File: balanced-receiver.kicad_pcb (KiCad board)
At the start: 2 copper layers, 52.5 x 40 mm, 54 parts, among them J1 NC3FAH2, J2 Barrel_Jack_Switch, J3 Screw_Terminal_01x02, J4 Screw_Terminal_01x02, J5 Screw_Terminal_01x02, J6 Screw_Terminal_01x02, J7 Screw_Terminal_01x02, J8 Conn_01x02_Pin, Q1 Q_PMOS_GDS, U1 THAT1240, U2 TPS62932, U3 LM2776

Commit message: Added DRC pipeline action
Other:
- board text added: "${COMMENT8} ${COMMENT9} ${REVISION} ${CURRENT_DATE}"
- board text removed: "Balanced Receiver ${COMMENT1} ${REVISION} ${CURRENT_DATE}"
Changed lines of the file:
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@@
 	(paper "A5")
 	(title_block
-		(title "Balanced Receiver")
-		(date "2025.01.31")
-		(rev "v1.0")
-		(company "Filip Tefr")
-		(comment 1 "github.com/brbcza")
+		(title "${TITLE_BLOCK_PROJECT_NAME}")
+		(date "${TITLE_BLOCK_DATE}")
+		(rev "${TITLE_BLOCK_REVISION}")
+		(company "${TITLE_BLOCK_AUTHOR}")
+		(comment 1 "${TITLE_BLOCK_REPOSITORY}")
+		(comment 8 "${TITLE_BLOCK_PROJECT_NAME_SHORT}")
+		(comment 9 "${TITLE_BLOCK_BASE_REPOSITORY}")
 	)
 	(layers
@@
 		(tags "neutrik xlr a")
 		(property "Reference" "J1"
-			(at 1.7 -8.1 360)
+			(at 1.7 -8.1 0)
 			(layer "F.SilkS")
 			(effects
@@
 		)
 		(property "Value" "NC3FAH2"
-			(at 4.3 18 360)
+			(at 4.3 18 0)
 			(layer "F.Fab")
 			(hide yes)
@@
 		)
 		(fp_text user "${REFERENCE}"
-			(at 10.35 3.81 360)
+			(at 10.35 3.81 0)
 			(layer "F.Fab")
 			(effects
@@
 		)
 	)
-	(gr_text "Balanced  Receiver\n${COMMENT1}\n${REVISION}  ${CURRENT_DATE}\n"
+	(gr_text "${COMMENT8}\n${COMMENT9}\n${REVISION}  ${CURRENT_DATE}\n"
 		(at 80.5325 53.44 0)
 		(layer "F.SilkS" knockout)

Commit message: Added release action
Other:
- board text added: "${COMMENT8} ${COMMENT9} ${REVISION} ${ISSUE_DATE}"
- board text removed: "${COMMENT8} ${COMMENT9} ${REVISION} ${CURRENT_DATE}"
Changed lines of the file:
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@@
 		)
 	)
-	(gr_text "${COMMENT8}\n${COMMENT9}\n${REVISION}  ${CURRENT_DATE}\n"
+	(gr_text "${COMMENT8}\n${COMMENT9}\n${REVISION} ${ISSUE_DATE}\n"
 		(at 80.5325 53.44 0)
 		(layer "F.SilkS" knockout)

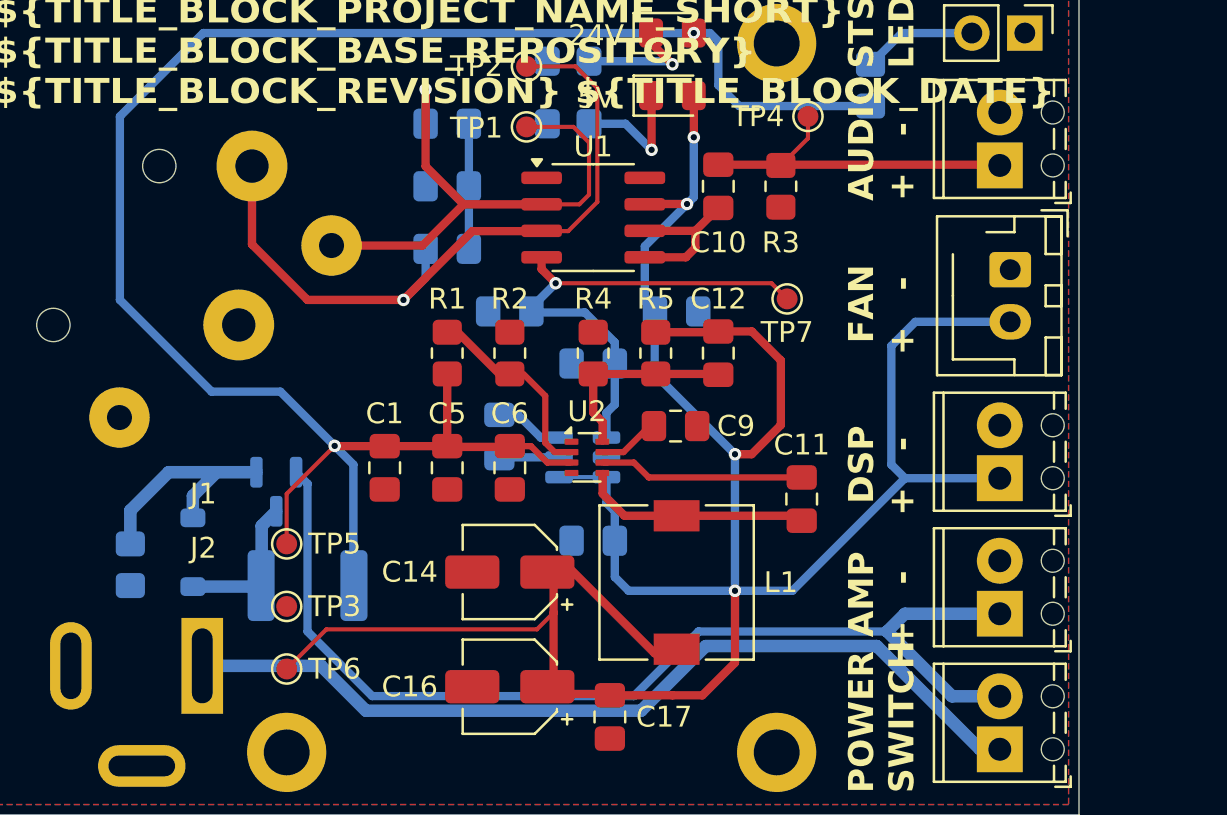
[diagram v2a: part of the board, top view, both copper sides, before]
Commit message: Added local component library
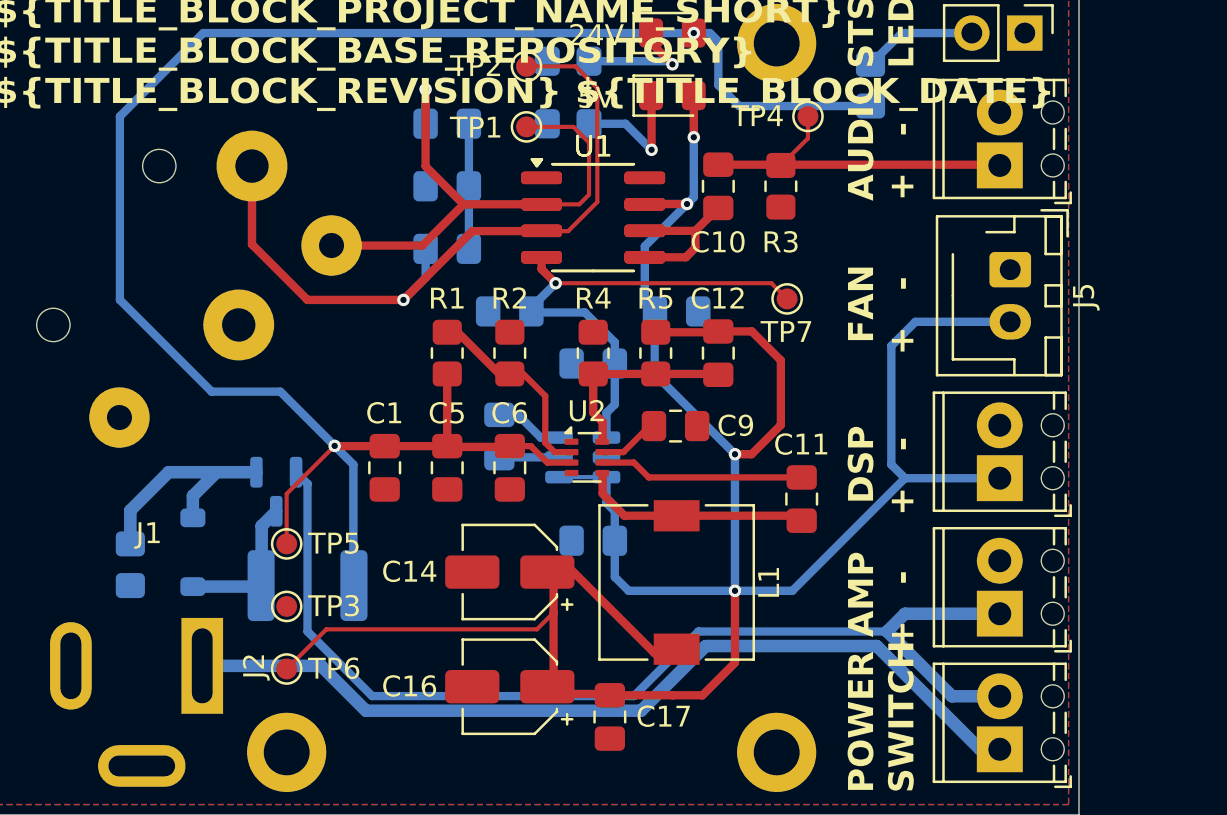
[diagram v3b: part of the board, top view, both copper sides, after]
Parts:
- added U1: THAT1240, Package_SO:SOIC-8_3.9x4.9mm_P1.27mm, F.Cu at (109.3, 58.8)
- F1: footprint brbCZa-KicadFootprintLib:Fuse_1812_4532Metric_Pad1.30x3.40mm_HandSolder -> balanced-receiver:Fuse_1812_4532Metric_Pad1.30x3.40mm_HandSolder
- J1: footprint brbCZa-KicadFootprintLib:Jack_XLR_Neutrik_NC3FAH2_Horizontal -> balanced-receiver:Jack_XLR_Neutrik_NC3FAH2_Horizontal
- J2: footprint brbCZa-KicadFootprintLib:BarrelJack_GCT_DCJ200-10-A_Horizontal -> balanced-receiver:BarrelJack_GCT_DCJ200-10-A_Horizontal
- J5: footprint brbCZa-KicadFootprintLib:JST_XH_B2B-XH-AM_1x02_P2.50mm_Vertical -> balanced-receiver:JST_XH_B2B-XH-AM_1x02_P2.50mm_Vertical
- L1: footprint brbCZa-KicadFootprintLib:L_7.3x7.3_H4.5 -> balanced-receiver:L_7.3x7.3_H4.5
- U2: footprint brbCZa-KicadFootprintLib:SOT-583-8 -> balanced-receiver:SOT-583-8

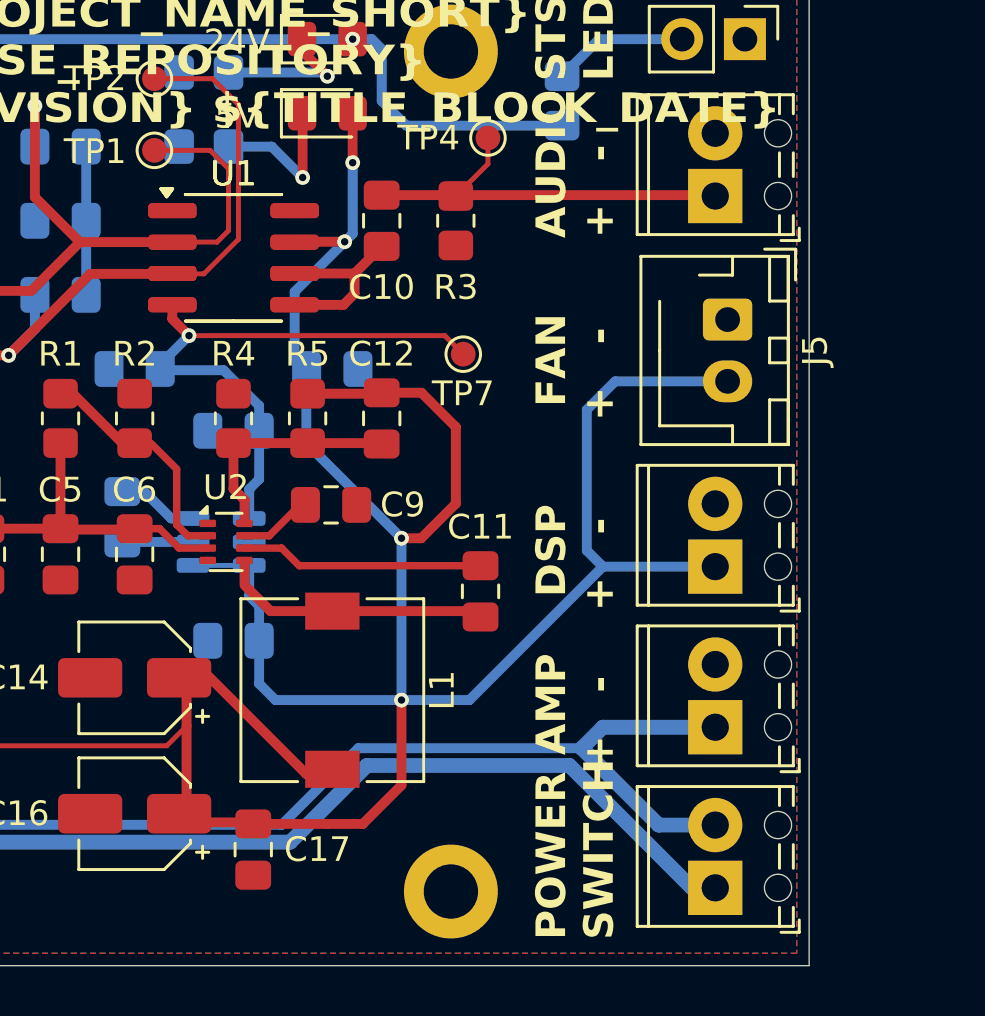
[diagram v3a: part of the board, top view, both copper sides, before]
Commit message: Fixed DRC and ERC errors
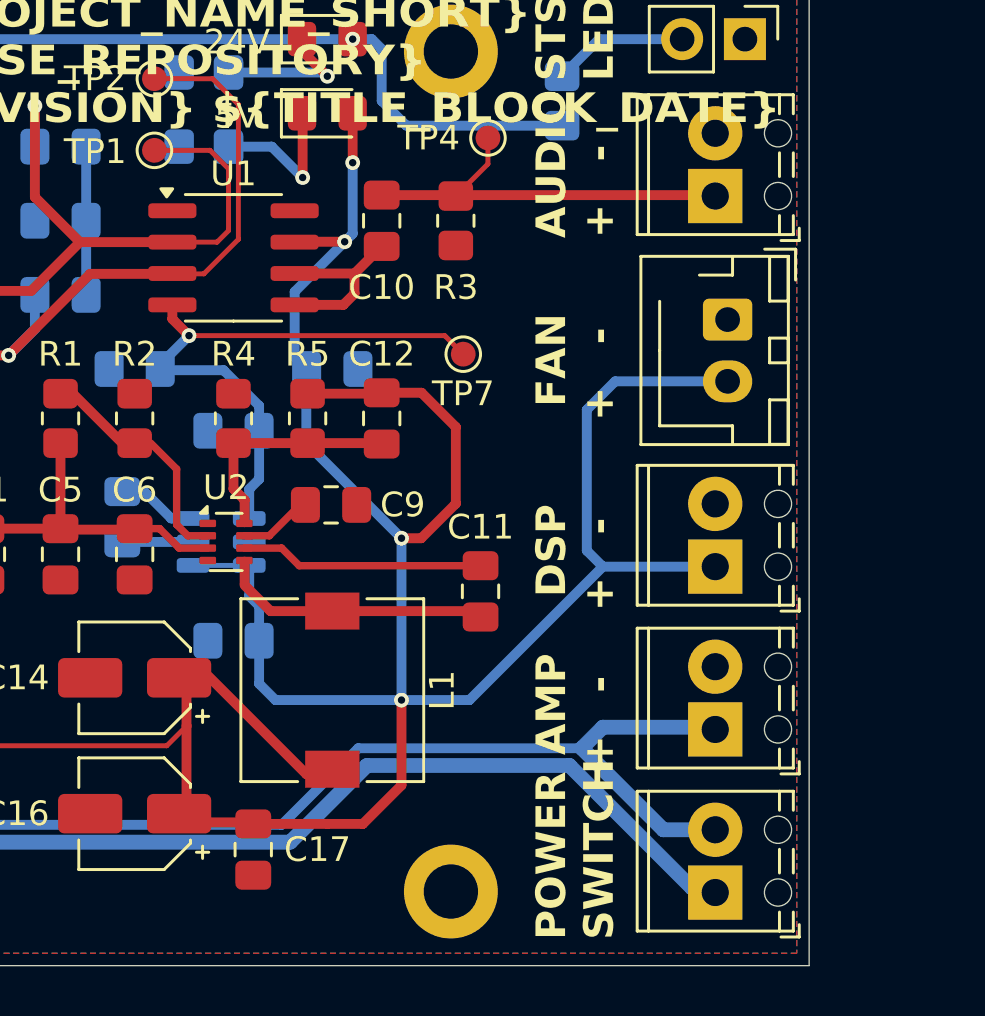
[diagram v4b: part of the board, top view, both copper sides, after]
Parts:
- removed the U1 at (109.3, 58.8)
- moved J3 0.19 mm to (128.8, 84.5)
- moved J4 0.09 mm to (128.8, 77.9)

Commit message: WIP: Converting to schematic
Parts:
- removed the C10 at (115.3, 57.3)
- removed the C4 at (102.3, 60.3)
- removed the C8 at (105.3, 63.3)
- removed D3: LED, LED_SMD:LED_0805_2012Metric_Pad1.15x1.40mm_HandSolder
- removed the J1 at (92.3, 63.9)
- removed J5: Screw_Terminal_01x02, balanced-receiver:JST_XH_B2B-XH-AM_1x02_P2.50mm_Vertical
- removed J8: Conn_01x02_Pin, Connector_PinHeader_2.54mm:PinHeader_1x02_P2.54mm_Vertical
- removed the R3 at (118.3, 57.3)
- removed the R7 at (122.6, 52.4)
- removed R9: 330Ω, Resistor_SMD:R_0805_2012Metric_Pad1.20x1.40mm_HandSolder
- removed the REF** at (118.1, 50.4)
- removed TP1: Audio+, TestPoint:TestPoint_Pad_D1.0mm
- removed the TP2 at (106.1, 51.5)
- removed TP3, TP7: -5V, TestPoint:TestPoint_Pad_D1.0mm
- removed TP4: AudioOut, TestPoint:TestPoint_Pad_D1.0mm
- removed TP6: +5V, TestPoint:TestPoint_Pad_D1.0mm
- added C17: 47pF, Capacitor_SMD:C_0805_2012Metric_Pad1.18x1.45mm_HandSolder, B.Cu at (28.4, 87.9)
- added C18: 470pF, Capacitor_SMD:C_0805_2012Metric_Pad1.18x1.45mm_HandSolder, B.Cu at (28.4, 85.4)
- added C19: 470pF, Capacitor_SMD:C_0805_2012Metric_Pad1.18x1.45mm_HandSolder, B.Cu at (28.4, 90.4)
- added C20: 100nF, Capacitor_SMD:C_0805_2012Metric_Pad1.18x1.45mm_HandSolder, F.Cu at (34.4, 80.4)
- added C21: 100nF, Capacitor_SMD:C_0805_2012Metric_Pad1.18x1.45mm_HandSolder, F.Cu at (34.4, 82.9)
- added C22: 1uF, Capacitor_SMD:C_0805_2012Metric_Pad1.18x1.45mm_HandSolder, F.Cu at (32.4, 69.9)
- added C23: 22pF, Capacitor_SMD:C_0805_2012Metric_Pad1.18x1.45mm_HandSolder, F.Cu at (57.4, 76.0)
- added C24: 22pF, Capacitor_SMD:C_0805_2012Metric_Pad1.18x1.45mm_HandSolder, F.Cu at (57.4, 71.9)
- added C25: 3.3nF, Capacitor_SMD:C_0805_2012Metric_Pad1.18x1.45mm_HandSolder, F.Cu at (60.9, 69.4)
- added C26: 56nF, Capacitor_SMD:C_0805_2012Metric_Pad1.18x1.45mm_HandSolder, F.Cu at (54.4, 66.9)
- added C27: 10uF, Capacitor_SMD:C_0805_2012Metric_Pad1.18x1.45mm_HandSolder, B.Cu at (42.9, 82.9)
- added C28: 100nF, Capacitor_SMD:C_0805_2012Metric_Pad1.18x1.45mm_HandSolder, F.Cu at (37.1, 75.4)
- added C29: 100nF, Capacitor_SMD:C_0805_2012Metric_Pad1.18x1.45mm_HandSolder, F.Cu at (39.4, 72.4)
- added C30: 100nF, Capacitor_SMD:C_0805_2012Metric_Pad1.18x1.45mm_HandSolder, B.Cu at (42.9, 75.4)
- added C31: 10uF, Capacitor_SMD:C_0805_2012Metric_Pad1.18x1.45mm_HandSolder, B.Cu at (42.9, 69.4)
- added C32: 100nF, Capacitor_SMD:C_0805_2012Metric_Pad1.18x1.45mm_HandSolder, B.Cu at (42.9, 77.9)
- added C33: 100nF, Capacitor_SMD:C_0805_2012Metric_Pad1.18x1.45mm_HandSolder, B.Cu at (42.9, 66.9)
- added C34: 100nF, Capacitor_SMD:C_0805_2012Metric_Pad1.18x1.45mm_HandSolder, B.Cu at (42.9, 80.4)
- added C35: 100nF, Capacitor_SMD:C_0805_2012Metric_Pad1.18x1.45mm_HandSolder, B.Cu at (47.4, 77.9)
- added C36: 10uF, Capacitor_SMD:C_0805_2012Metric_Pad1.18x1.45mm_HandSolder, B.Cu at (47.4, 80.4)
- added C37: 100nF, Capacitor_SMD:C_0805_2012Metric_Pad1.18x1.45mm_HandSolder, B.Cu at (54.4, 66.9)
- added C38: 100nF, Capacitor_SMD:C_0805_2012Metric_Pad1.18x1.45mm_HandSolder, B.Cu at (49.9, 66.9)
- added C39: 10uF, Capacitor_SMD:C_0805_2012Metric_Pad1.18x1.45mm_HandSolder, B.Cu at (54.4, 69.4)
- added C40: 10uF, Capacitor_SMD:C_0805_2012Metric_Pad1.18x1.45mm_HandSolder, B.Cu at (49.9, 69.4)
- added C41: 1uF, Capacitor_SMD:C_0805_2012Metric_Pad1.18x1.45mm_HandSolder, F.Cu at (28.9, 61.8)
- added C42: 1uF, Capacitor_SMD:C_0805_2012Metric_Pad1.18x1.45mm_HandSolder, F.Cu at (63.9, 57.3)
- added C43: 820pF, Capacitor_SMD:C_0805_2012Metric_Pad1.18x1.45mm_HandSolder, F.Cu at (34.9, 57.3)
- added C44: 820pF, Capacitor_SMD:C_0805_2012Metric_Pad1.18x1.45mm_HandSolder, F.Cu at (57.9, 61.8)
- added C45: 680pF, Capacitor_SMD:C_0805_2012Metric_Pad1.18x1.45mm_HandSolder, F.Cu at (31.9, 57.3)
- added C46: 680pF, Capacitor_SMD:C_0805_2012Metric_Pad1.18x1.45mm_HandSolder, F.Cu at (60.9, 61.8)
- added C47: 100nF, Capacitor_SMD:C_0805_2012Metric_Pad1.18x1.45mm_HandSolder, B.Cu at (49.4, 43.9)
- added C48: 100nF, Capacitor_SMD:C_0805_2012Metric_Pad1.18x1.45mm_HandSolder, B.Cu at (43.4, 50.5)
- added C49: 100nF, Capacitor_SMD:C_0805_2012Metric_Pad1.18x1.45mm_HandSolder, B.Cu at (49.4, 57.4)
- added C50: 100nF, Capacitor_SMD:C_0805_2012Metric_Pad1.18x1.45mm_HandSolder, B.Cu at (43.9, 62.4)
- added C51: 1uF, Capacitor_SMD:C_0805_2012Metric_Pad1.18x1.45mm_HandSolder, F.Cu at (28.9, 50.5)
- added C52: 1uF, Capacitor_SMD:C_0805_2012Metric_Pad1.18x1.45mm_HandSolder, F.Cu at (63.9, 46.0)
- added C53: 820pF, Capacitor_SMD:C_0805_2012Metric_Pad1.18x1.45mm_HandSolder, F.Cu at (34.9, 46.0)
- added C54: 820pF, Capacitor_SMD:C_0805_2012Metric_Pad1.18x1.45mm_HandSolder, F.Cu at (57.9, 50.5)
- added C55: 680pF, Capacitor_SMD:C_0805_2012Metric_Pad1.18x1.45mm_HandSolder, F.Cu at (31.9, 46.0)
- added C56: 680pF, Capacitor_SMD:C_0805_2012Metric_Pad1.18x1.45mm_HandSolder, F.Cu at (60.9, 50.5)
- added C57: 100nF, Capacitor_SMD:C_0805_2012Metric_Pad1.18x1.45mm_HandSolder, F.Cu at (44.9, 83.4)
- added C58: 10uF, Capacitor_SMD:C_0805_2012Metric_Pad1.18x1.45mm_HandSolder, B.Cu at (55.4, 88.6)
- added C59: 10uF, Capacitor_SMD:C_0805_2012Metric_Pad1.18x1.45mm_HandSolder, B.Cu at (55.4, 90.9)
- added C6: 10uF, Capacitor_SMD:C_0805_2012Metric_Pad1.18x1.45mm_HandSolder, B.Cu at (65.4, 97.4)
- added C60: 10uF, Capacitor_SMD:C_0805_2012Metric_Pad1.18x1.45mm_HandSolder, B.Cu at (49.4, 46.4)
- added C61: 10uF, Capacitor_SMD:C_0805_2012Metric_Pad1.18x1.45mm_HandSolder, B.Cu at (43.9, 59.9)
- added C62: 10uF, Capacitor_SMD:C_0805_2012Metric_Pad1.18x1.45mm_HandSolder, B.Cu at (43.4, 52.9)
- added C63: 10uF, Capacitor_SMD:C_0805_2012Metric_Pad1.18x1.45mm_HandSolder, B.Cu at (49.4, 54.9)
- added J10: Conn_01x03_Pin, Connector_JST:JST_XH_B3B-XH-A_1x03_P2.50mm_Vertical, F.Cu at (77.4, 32.9)
- added J11: Conn_01x04_Pin, Connector_PinHeader_2.54mm:PinHeader_1x04_P2.54mm_Vertical, F.Cu at (70.8, 59.9)
- added J12: Conn_01x04_Pin, Connector_PinHeader_2.54mm:PinHeader_1x04_P2.54mm_Vertical, F.Cu at (70.8, 57.4)
- added J13: Conn_01x04_Pin, Connector_PinHeader_2.54mm:PinHeader_1x04_P2.54mm_Vertical, F.Cu at (70.8, 54.9)
- added J3: Screw_Terminal_01x02, balanced-receiver:JST_XH_B2B-XH-AM_1x02_P2.50mm_Vertical, F.Cu at (77.7, 104.4)
- added J9: Conn_01x03_Pin, Connector_JST:JST_XH_B3B-XH-A_1x03_P2.50mm_Vertical, F.Cu at (77.4, 44.4)
- added L2: 1uH, Inductor_SMD:L_0805_2012Metric_Pad1.05x1.20mm_HandSolder, B.Cu at (55.4, 86.4)
- added L3: 1uH, Inductor_SMD:L_0805_2012Metric_Pad1.05x1.20mm_HandSolder, B.Cu at (55.4, 93.1)
- added R10: 10kΩ, Resistor_SMD:R_0805_2012Metric_Pad1.20x1.40mm_HandSolder, F.Cu at (32.4, 67.4)
- added R11: 100Ω, Resistor_SMD:R_0805_2012Metric_Pad1.20x1.40mm_HandSolder, F.Cu at (54.4, 75.9)
- added R12: 475Ω, Resistor_SMD:R_0805_2012Metric_Pad1.20x1.40mm_HandSolder, F.Cu at (60.9, 66.9)
- added R13: 10k, Resistor_SMD:R_0805_2012Metric_Pad1.20x1.40mm_HandSolder, F.Cu at (37.1, 77.9)
- added R14: 7kΩ, Resistor_SMD:R_0805_2012Metric_Pad1.20x1.40mm_HandSolder, F.Cu at (39.4, 67.4)
- added R15: 18kΩ, Resistor_SMD:R_0805_2012Metric_Pad1.20x1.40mm_HandSolder, F.Cu at (39.4, 69.9)
- added R16: 2.2kΩ, Resistor_SMD:R_0805_2012Metric_Pad1.20x1.40mm_HandSolder, F.Cu at (54.4, 81.9)
- added R17: 2.2kΩ, Resistor_SMD:R_0805_2012Metric_Pad1.20x1.40mm_HandSolder, F.Cu at (60.4, 81.9)
- added R18: 10kΩ, Resistor_SMD:R_0805_2012Metric_Pad1.20x1.40mm_HandSolder, F.Cu at (57.4, 81.9)
- added R19: 10kΩ, Resistor_SMD:R_0805_2012Metric_Pad1.20x1.40mm_HandSolder, F.Cu at (31.9, 61.8)
- added R20: 10kΩ, Resistor_SMD:R_0805_2012Metric_Pad1.20x1.40mm_HandSolder, F.Cu at (60.9, 57.3)
- added R21: 6.2kΩ, Resistor_SMD:R_0805_2012Metric_Pad1.20x1.40mm_HandSolder, F.Cu at (34.9, 61.8)
- added R22: 6.2kΩ, Resistor_SMD:R_0805_2012Metric_Pad1.20x1.40mm_HandSolder, F.Cu at (57.9, 57.3)
- added R23: 8.2kΩ, Resistor_SMD:R_0805_2012Metric_Pad1.20x1.40mm_HandSolder, F.Cu at (37.9, 61.8)
- added R24: 8.2kΩ, Resistor_SMD:R_0805_2012Metric_Pad1.20x1.40mm_HandSolder, F.Cu at (54.9, 57.3)
- added R25: 10kΩ, Resistor_SMD:R_0805_2012Metric_Pad1.20x1.40mm_HandSolder, F.Cu at (37.9, 57.3)
- added R26: 10kΩ, Resistor_SMD:R_0805_2012Metric_Pad1.20x1.40mm_HandSolder, F.Cu at (54.9, 61.8)
- added R27: 10kΩ, Resistor_SMD:R_0805_2012Metric_Pad1.20x1.40mm_HandSolder, F.Cu at (40.9, 57.3)
- added R28: 10kΩ, Resistor_SMD:R_0805_2012Metric_Pad1.20x1.40mm_HandSolder, F.Cu at (51.9, 61.8)
- added R29: 10kΩ, Resistor_SMD:R_0805_2012Metric_Pad1.20x1.40mm_HandSolder, F.Cu at (31.9, 50.5)
- added R30: 10kΩ, Resistor_SMD:R_0805_2012Metric_Pad1.20x1.40mm_HandSolder, F.Cu at (60.9, 46.0)
- added R31: 6.2kΩ, Resistor_SMD:R_0805_2012Metric_Pad1.20x1.40mm_HandSolder, F.Cu at (34.9, 50.5)
- added R32: 6.2kΩ, Resistor_SMD:R_0805_2012Metric_Pad1.20x1.40mm_HandSolder, F.Cu at (57.9, 46.0)
- added R33: 8.2kΩ, Resistor_SMD:R_0805_2012Metric_Pad1.20x1.40mm_HandSolder, F.Cu at (37.9, 50.5)
- added R34: 8.2kΩ, Resistor_SMD:R_0805_2012Metric_Pad1.20x1.40mm_HandSolder, F.Cu at (54.9, 46.0)
- added R35: 10kΩ, Resistor_SMD:R_0805_2012Metric_Pad1.20x1.40mm_HandSolder, F.Cu at (37.9, 46.0)
- added R36: 10kΩ, Resistor_SMD:R_0805_2012Metric_Pad1.20x1.40mm_HandSolder, F.Cu at (54.9, 50.5)
- added R37: 10kΩ, Resistor_SMD:R_0805_2012Metric_Pad1.20x1.40mm_HandSolder, F.Cu at (40.9, 46.0)
- added R38: 10kΩ, Resistor_SMD:R_0805_2012Metric_Pad1.20x1.40mm_HandSolder, F.Cu at (51.9, 50.5)
- added REF**: MountingHole_2.2mm_M2_DIN965_Pad, MountingHole:MountingHole_2.2mm_M2_DIN965_Pad, F.Cu at (64.4, 38.9)
- added REF**: MountingHole_2.2mm_M2_DIN965_Pad, MountingHole:MountingHole_2.2mm_M2_DIN965_Pad, F.Cu at (40.4, 38.9)
- added U2: LM1117DT-1.8, Package_TO_SOT_SMD:SOT-223-3_TabPin2, B.Cu at (63.2, 91.4)
- added U5: THAT1240, Package_SO:SOIC-8_3.9x4.9mm_P1.27mm, F.Cu at (29.4, 77.9)
- added U6: ADAU1701, Package_QFP:LQFP-48_7x7mm_P0.5mm, F.Cu at (47.6, 73.2)
- added U7: 24LC256, Package_SO:SOIC-8_3.9x4.9mm_P1.27mm, F.Cu at (48.0, 88.5)
- added U8: OPA1612AxD, Package_SO:SOIC-8_3.9x4.9mm_P1.27mm, F.Cu at (46.4, 59.8)
- added U9: OPA1612AxD, Package_SO:SOIC-8_3.9x4.9mm_P1.27mm, F.Cu at (46.4, 48.5)
- added Y1: 12.288 MHz, balanced-receiver:Crystal_SMD_7050-4Pin_7.0x5.0mm, F.Cu at (63.4, 74.4)
- C2: value 47pF -> 10uF
- C3: value 470pF -> 10uF
- C7: value 100nF -> 10uF
- J2: renamed from J3; footprint TerminalBlock_Phoenix:TerminalBlock_Phoenix_MPT-0,5-2-2.54_1x02_P2.54mm_Horizontal -> balanced-receiver:TerminalBlock_Phoenix_MPT-0,5-2-2.54_1x02_P2.54mm_Horizontal
- J4: value Screw_Terminal_01x02 -> Screw_Terminal_01x03; footprint TerminalBlock_Phoenix:TerminalBlock_Phoenix_MPT-0,5-2-2.54_1x02_P2.54mm_Horizontal -> balanced-receiver:TerminalBlock_1x03_P7.50mm_Horizontal
- J6: value Screw_Terminal_01x02 -> NC3FAH2; footprint TerminalBlock_Phoenix:TerminalBlock_Phoenix_MPT-0,5-2-2.54_1x02_P2.54mm_Horizontal -> balanced-receiver:Jack_XLR_Neutrik_NC3FAH2_Horizontal
- J7: value Screw_Terminal_01x02 -> Conn_02x04_Odd_Even; footprint TerminalBlock_Phoenix:TerminalBlock_Phoenix_MPT-0,5-2-2.54_1x02_P2.54mm_Horizontal -> Connector_PinHeader_2.54mm:PinHeader_2x04_P2.54mm_Vertical
- L1: footprint balanced-receiver:L_7.3x7.3_H4.5 -> Inductor_SMD:L_APV_APH0530
- U1: value THAT1240 -> LM1117DT-3.3; footprint Package_SO:SOIC-8_3.9x4.9mm_P1.27mm -> Package_TO_SOT_SMD:SOT-223-3_TabPin2; moved to B.Cu
- U4: renamed from U3; footprint Package_TO_SOT_SMD:SOT-23-6 -> Package_TO_SOT_SMD:SOT-23-6_Handsoldering
- moved J6 93.5 mm to (38.2, 94.4), turned to 180 degrees
- moved D2 78.9 mm to (68.2, 114.8), turned to 90 degrees
- moved R7 75.0 mm to (68.2, 114.7), turned to 90 degrees
- moved C10 67.3 mm to (58.9, 101.9), turned to 180 degrees
- moved U1 63.5 mm to (63.3, 102.4)
- moved C8 62.4 mm to (58.9, 99.4)
- moved C1 62.2 mm to (45.1, 101.3)
- moved C11 62.2 mm to (50.6, 99.8)
- moved C12 62.2 mm to (61.1, 95.8)
- moved C13 62.2 mm to (51.1, 106.3)
- moved C14 62.2 mm to (51.1, 111.8)
- moved C4 62.2 mm to (48.1, 101.3)
- moved C5 62.2 mm to (51.1, 101.3)
- moved D1 62.2 mm to (35.9, 105.3)
- moved F1 62.2 mm to (41.4, 106.9)
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- renumbered C11 to C10, C15 to C11, C14 to C13, C16 to C14, C17 to C15, C18 to C16, C5 to C4, C6 to C5, C9 to C8, C13 to C9, J2 to J1, R4 to R3, R6 to R4, R8 to R7, TP5 to TP2, U2 to U3
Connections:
- C16 pad 1: -5V -> Net-(U4-VOUT)
- C2 pad 2: Net-(C2-Pad2) -> +5V
- C3 pad 1: /Audio- -> GND
- C3 pad 2: Net-(C2-Pad2) -> +5V
- C7 pad 1: +5V -> GND
- C7 pad 2: GND -> +1.8V
- J1 pad 1: Net-(J3-Pin_1) -> VCC_UN
- J2 pad 1: Net-(J3-Pin_1) -> VCC_UN
- J4 pad 1: VCC -> GND
- J4 pad 2: GND -> VCC_UN
- J6 pad 1: +5V -> GND
- J6 pad 2: GND -> /analog_input/Audio+
- J7 pad 1: /AudioOut -> /adau_1701/SCL
- U1 pad 2: /Audio- -> +3.3V
- U1 pad 3: /Audio+ -> +5V
- U4 pad 1: -5V -> Net-(U4-VOUT)
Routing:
- net +3.3V: track 0.00 -> 175.0 mm, vias 0 -> 5
- net +5V_ANALOG: track 0.00 -> 87.1 mm, vias 0 -> 3
- net VCC_UN: track 0.00 -> 70.0 mm
- net /analog_output/AUDIO_OUT_1: track 0.00 -> 66.3 mm, vias 0 -> 1
- net /analog_output/AUDIO_OUT_0: track 0.00 -> 65.1 mm, vias 0 -> 1
- net /adau_1701/WP: track 0.00 -> 59.1 mm, vias 0 -> 2
- net /analog_output/AUDIO_OUT_2: track 0.00 -> 58.1 mm, vias 0 -> 1
- net -5V: track 23.6 -> 79.7 mm, vias 1 -> 3
- net /analog_output/AUDIO_OUT_3: track 0.00 -> 52.7 mm, vias 0 -> 1
- net /adau_1701/SDA: track 0.00 -> 50.1 mm, vias 0 -> 4
- net +1.8V: track 0.00 -> 49.3 mm, vias 0 -> 3
- net /adau_1701/SCL: track 0.00 -> 45.8 mm, vias 0 -> 2
- net Net-(J3-Pin_1): track 42.5 -> 0.00 mm
- net /Audio+: track 35.6 -> 0.00 mm, vias 1 -> 0
- net ADAU_AUDIO_OUTPUT_3: track 0.00 -> 34.5 mm, vias 0 -> 2
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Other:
- board size 52.5 x 40 mm -> 55.5 x 89 mm
- board text added: "3.3V"
- board text added: "AMP SW + -"
- board text added: "AUDIO A0 - A2"
- board text added: "AUDIO A1 - A3"
- board text added: "GND"
- board text added: "M2"
- board text added: "M3"
- board text added: "M8"
- board text added: "M9"
- board text added: "PWR"
- board text added: "SCL"
- board text added: "SDA"
- board text added: "WP"
- board text added: "{ "ViaStitching": "0.2", "stitch_zone_0": { "HSpacing": "5", "VSpacing": "5", "HOffset": "0", "VOffset": "0", "Clearance": "0", "Randomize": false } }"
- board text removed: "24V"
- board text removed: "AMP + -"
- board text removed: "AUDIO + -"
- board text removed: "DSP + -"
- board text removed: "STS LED"
- board text removed: "{ "ViaStitching": "0.2", "stitch_zone_0": { "HSpacing": "5", "VSpacing": "5", "Clearance": "0", "Randomize": false }, "stitch_zone_1": { "HSpacing": "5", "VSpacing": "5", "Clearance": "0", "Randomize": false } }"

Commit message: Update workflows and configurations for balanced-receiver project
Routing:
- net GND: vias 9 -> 63
